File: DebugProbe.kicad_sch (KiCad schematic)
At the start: 36 parts, among them J5 DBG_PRGM, J6 UART_DBG, J7 DGB Exp. Header, U4 25Q32, U5 RP2040, Y1 12MHz

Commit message: Renamed files.
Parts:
- J5: symbol rp2040-launchpad-PCB:Jumper -> rp2350b-launchpad-PCB:Jumper
- U4: symbol rp2040-launchpad-PCB:25Q32 -> rp2350b-launchpad-PCB:25Q32
- U5: symbol rp2040-launchpad-PCB:RP2040 -> rp2350b-launchpad-PCB:RP2040
- USB1: symbol rp2040-launchpad-PCB:USB-C-Socket -> rp2350b-launchpad-PCB:USB-C-Socket
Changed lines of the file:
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@@
 	)
 	(symbol
-		(lib_id "rp2040-launchpad-PCB:25Q32")
+		(lib_id "rp2350b-launchpad-PCB:25Q32")
 		(at 93.98 135.89 0)
 		(mirror y)
@@
 	)
 	(symbol
-		(lib_id "rp2040-launchpad-PCB:RP2040")
+		(lib_id "rp2350b-launchpad-PCB:RP2040")
 		(at 139.7 105.41 0)
 		(unit 1)
@@
 	)
 	(symbol
-		(lib_id "rp2040-launchpad-PCB:Jumper")
+		(lib_id "rp2350b-launchpad-PCB:Jumper")
 		(at 102.87 151.13 0)
 		(unit 1)
@@
 	)
 	(symbol
-		(lib_id "rp2040-launchpad-PCB:+3V3_DBG")
+		(lib_id "rp2350b-launchpad-PCB:+3V3_DBG")
 		(at 196.85 52.07 0)
 		(unit 1)
@@
 	)
 	(symbol
-		(lib_id "rp2040-launchpad-PCB:GND_DBG")
+		(lib_id "rp2350b-launchpad-PCB:GND_DBG")
 		(at 223.52 85.09 0)
 		(unit 1)
@@
 	)
 	(symbol
-		(lib_id "rp2040-launchpad-PCB:+3V3_DBG")
+		(lib_id "rp2350b-launchpad-PCB:+3V3_DBG")
 		(at 80.01 128.27 0)
 		(unit 1)
@@
 	)
 	(symbol
-		(lib_id "rp2040-launchpad-PCB:GND_DBG")
+		(lib_id "rp2350b-launchpad-PCB:GND_DBG")
 		(at 88.9 59.69 0)
 		(unit 1)
@@
 	)
 	(symbol
-		(lib_id "rp2040-launchpad-PCB:GND_DBG")
+		(lib_id "rp2350b-launchpad-PCB:GND_DBG")
 		(at 80.01 152.4 0)
 		(unit 1)
@@
 	)
 	(symbol
-		(lib_id "rp2040-launchpad-PCB:GND_DBG")
+		(lib_id "rp2350b-launchpad-PCB:GND_DBG")
 		(at 134.62 152.4 0)
 		(unit 1)
@@
 	)
 	(symbol
-		(lib_id "rp2040-launchpad-PCB:GND_DBG")
+		(lib_id "rp2350b-launchpad-PCB:GND_DBG")
 		(at 120.65 59.69 0)
 		(unit 1)
@@
 	)
 	(symbol
-		(lib_id "rp2040-launchpad-PCB:GND_DBG")
+		(lib_id "rp2350b-launchpad-PCB:GND_DBG")
 		(at 80.01 110.49 0)
 		(unit 1)
@@
 	)
 	(symbol
-		(lib_id "rp2040-launchpad-PCB:+3V3_DBG")
+		(lib_id "rp2350b-launchpad-PCB:+3V3_DBG")
 		(at 143.51 151.13 270)
 		(unit 1)
@@
 	)
 	(symbol
-		(lib_id "rp2040-launchpad-PCB:GND_DBG")
+		(lib_id "rp2350b-launchpad-PCB:GND_DBG")
 		(at 99.06 104.14 90)
 		(unit 1)
@@
 	)
 	(symbol
-		(lib_id "rp2040-launchpad-PCB:GND_DBG")
+		(lib_id "rp2350b-launchpad-PCB:GND_DBG")
 		(at 212.09 123.19 180)
 		(unit 1)
@@
 	)
 	(symbol
-		(lib_id "rp2040-launchpad-PCB:+3V3_DBG")
+		(lib_id "rp2350b-launchpad-PCB:+3V3_DBG")
 		(at 196.85 123.19 0)
 		(unit 1)
@@
 	)
 	(symbol
-		(lib_id "rp2040-launchpad-PCB:+3V3_DBG")
+		(lib_id "rp2350b-launchpad-PCB:+3V3_DBG")
 		(at 113.03 121.92 90)
 		(unit 1)
@@
 	)
 	(symbol
-		(lib_id "rp2040-launchpad-PCB:+3V3_DBG")
+		(lib_id "rp2350b-launchpad-PCB:+3V3_DBG")
 		(at 119.38 151.13 270)
 		(unit 1)
@@
 	)
 	(symbol
-		(lib_id "rp2040-launchpad-PCB:GND_DBG")
+		(lib_id "rp2350b-launchpad-PCB:GND_DBG")
 		(at 196.85 59.69 0)
 		(unit 1)
@@
 		)
 		(instances
-			(project "rp2040-launchpad-PCB"
+			(project "rp2350b-launchpad-PCB"
 				(path "/60290668-847e-40fe-8544-1cbbc26023b6/00000000-0000-0000-0000-00006225139f"
 					(reference "R6")
@@
 	)
 	(symbol
-		(lib_id "rp2040-launchpad-PCB:GND_DBG")
+		(lib_id "rp2350b-launchpad-PCB:GND_DBG")
 		(at 59.69 109.22 0)
 		(unit 1)
@@
 		)
 		(instances
-			(project "rp2040-launchpad-PCB"
+			(project "rp2350b-launchpad-PCB"
 				(path "/60290668-847e-40fe-8544-1cbbc26023b6/00000000-0000-0000-0000-00006225139f"
 					(reference "#PWR010")
@@
 		)
 		(instances
-			(project "rp2040-launchpad-PCB"
+			(project "rp2350b-launchpad-PCB"
 				(path "/60290668-847e-40fe-8544-1cbbc26023b6/00000000-0000-0000-0000-00006225139f"
 					(reference "R7")
@@
 		)
 		(instances
-			(project "rp2040-launchpad-PCB"
+			(project "rp2350b-launchpad-PCB"
 				(path "/60290668-847e-40fe-8544-1cbbc26023b6/00000000-0000-0000-0000-00006225139f"
 					(reference "R8")
@@
 	)
 	(symbol
-		(lib_id "rp2040-launchpad-PCB:USB-C-Socket")
+		(lib_id "rp2350b-launchpad-PCB:USB-C-Socket")
 		(at 57.15 87.63 0)
 		(unit 1)

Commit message: More fixes...
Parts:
- U5: footprint rp2350-launchpad:QFN40P700X700X90-57N -> rp2350b-launchpad-PCB:QFN40P700X700X90-57N
- USB1: footprint rp2350-launchpad:USB-C-GCT-USB4105 -> rp2350b-launchpad-PCB:USB-C-GCT-USB4105
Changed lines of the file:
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@@
 			)
 		)
-		(property "Footprint" "rp2350-launchpad:QFN40P700X700X90-57N"
+		(property "Footprint" "rp2350b-launchpad-PCB:QFN40P700X700X90-57N"
 			(at 179.07 99.06 0)
 			(effects
@@
 			)
 		)
-		(property "Footprint" "rp2350-launchpad:USB-C-GCT-USB4105"
+		(property "Footprint" "rp2350b-launchpad-PCB:USB-C-GCT-USB4105"
 			(at 59.69 78.74 0)
 			(effects

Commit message: Footprint cleanup.
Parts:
- U5: footprint rp2350b-launchpad-PCB:QFN40P700X700X90-57N -> Package_DFN_QFN:QFN-56-1EP_7x7mm_P0.4mm_EP3.2x3.2mm_ThermalVias
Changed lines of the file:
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@@
 			)
 		)
-		(property "Footprint" "rp2350b-launchpad-PCB:QFN40P700X700X90-57N"
+		(property "Footprint" "Package_DFN_QFN:QFN-56-1EP_7x7mm_P0.4mm_EP3.2x3.2mm_ThermalVias"
 			(at 179.07 99.06 0)
 			(effects

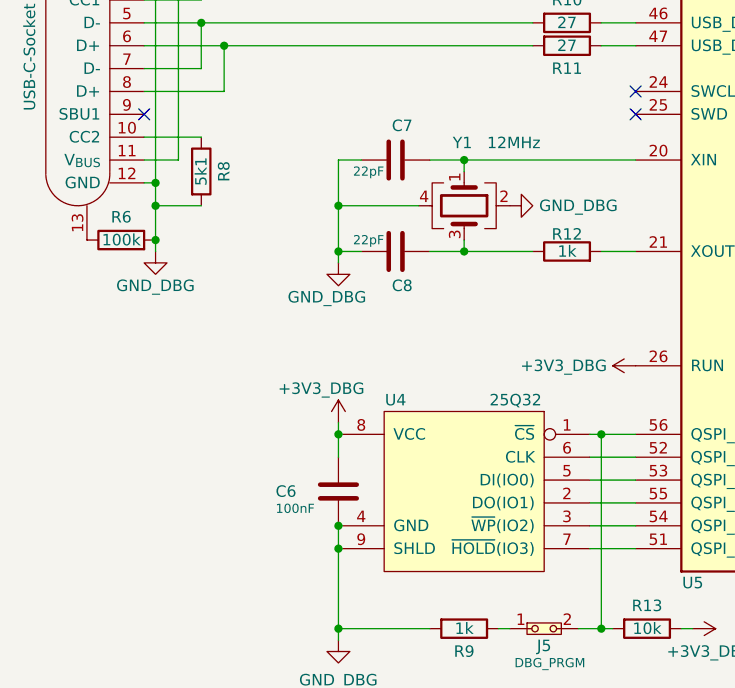
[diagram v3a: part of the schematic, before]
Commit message: Ready for Version v1.0. Changed PCB to comply with RPi design 'rules'. Without using special components and PCB designs, the PCB may not be produced :\
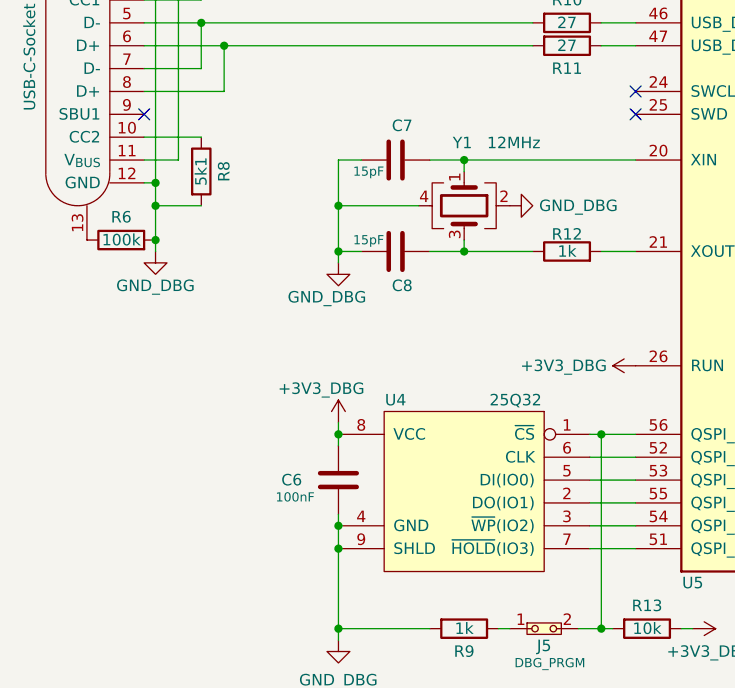
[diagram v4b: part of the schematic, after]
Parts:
- C7, C8: value 22pF -> 15pF
- U5: footprint Package_DFN_QFN:QFN-56-1EP_7x7mm_P0.4mm_EP3.2x3.2mm_ThermalVias -> Package_DFN_QFN:QFN-56-1EP_7x7mm_P0.4mm_EP3.2x3.2mm
- USB1: footprint rp2350b-launchpad-PCB:USB-C-GCT-USB4105 -> rp2350b-launchpad-PCB:GT-USB-7010B
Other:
- company: (none) -> ISS Intelligent Sensor Solutions
- title: (none) -> RP2350 Launchpad
- moved on the sheet: C6
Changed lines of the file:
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@@
 	(generator_version "8.0")
 	(paper "A4")
+	(title_block
+		(title "RP2350 Launchpad")
+		(date "2024-12-10")
+		(rev "v1.0")
+		(company "ISS Intelligent Sensor Solutions")
+		(comment 1 "(C) 2024 A. Terstegge")
+		(comment 2 "and integrated RP2040-based debugger")
+		(comment 3 "A TI-style Launchpad with RP2350 MCU")
+	)
 	(junction
 		(at 64.77 83.82)
@@
 	)
 	(junction
+		(at 80.01 129.54)
+		(diameter 0)
+		(color 0 0 0 0)
+	)
+	(junction
 		(at 137.16 52.07)
 		(diameter 0)
@@
 	)
 	(junction
-		(at 80.01 139.7)
-		(diameter 0)
-		(color 0 0 0 0)
-	)
-	(junction
 		(at 177.8 52.07)
 		(diameter 0)
@@
 	)
 	(junction
-		(at 165.1 59.69)
+		(at 80.01 139.7)
 		(diameter 0)
 		(color 0 0 0 0)
 	)
 	(junction
-		(at 190.5 52.07)
+		(at 165.1 59.69)
 		(diameter 0)
 		(color 0 0 0 0)
 	)
 	(junction
-		(at 109.22 151.13)
+		(at 190.5 52.07)
 		(diameter 0)
 		(color 0 0 0 0)
 	)
 	(junction
-		(at 95.25 59.69)
+		(at 109.22 151.13)
 		(diameter 0)
 		(color 0 0 0 0)
 	)
 	(junction
-		(at 80.01 129.54)
+		(at 95.25 59.69)
 		(diameter 0)
 		(color 0 0 0 0)
@@
 	(wire
 		(pts
+			(xy 80.01 129.54) (xy 80.01 130.81)
+		)
+		(stroke
+			(width 0)
+			(type default)
+		)
+	)
+	(wire
+		(pts
 			(xy 59.69 104.14) (xy 64.77 104.14)
 		)
@@
 	(wire
 		(pts
-			(xy 80.01 132.08) (xy 80.01 129.54)
-		)
-		(stroke
-			(width 0)
-			(type default)
-		)
-	)
-	(wire
-		(pts
 			(xy 210.82 139.7) (xy 222.25 139.7)
 		)
@@
 	(wire
 		(pts
+			(xy 80.01 138.43) (xy 80.01 139.7)
+		)
+		(stroke
+			(width 0)
+			(type default)
+		)
+	)
+	(wire
+		(pts
 			(xy 107.95 139.7) (xy 113.03 139.7)
 		)
@@
 	(symbol
 		(lib_id "Device:C")
-		(at 80.01 135.89 0)
+		(at 80.01 134.62 0)
 		(unit 1)
 		(exclude_from_sim no)
@@
 		(dnp no)
 		(property "Reference" "C6"
-			(at 73.025 135.89 0)
+			(at 73.66 134.62 0)
 			(effects
 				(font
@@
 		)
 		(property "Value" "100nF"
-			(at 73.025 137.795 0)
+			(at 73.025 136.525 0)
 			(effects
 				(font
@@
 		)
 		(property "Footprint" "Capacitor_SMD:C_0603_1608Metric"
-			(at 80.01 135.89 0)
+			(at 80.01 134.62 0)
 			(effects
 				(font
@@
 		)
 		(property "Datasheet" "https://www.digikey.de/de/products/detail/kemet/C0603C104J4RAC7013/8572406"
-			(at 80.01 135.89 0)
+			(at 80.01 134.62 0)
 			(effects
 				(font
@@
 		)
 		(property "Description" ""
-			(at 80.01 135.89 0)
+			(at 80.01 134.62 0)
 			(effects
 				(font
@@
 		)
 		(property "MANUFACTURER" "z.B. Kemet"
-			(at 80.01 135.89 0)
+			(at 80.01 134.62 0)
 			(effects
 				(font
@@
 		)
 		(property "STANDARD" "unkritisch"
-			(at 80.01 135.89 0)
+			(at 80.01 134.62 0)
 			(effects
 				(font
@@
 			)
 		)
-		(property "Footprint" "Package_DFN_QFN:QFN-56-1EP_7x7mm_P0.4mm_EP3.2x3.2mm_ThermalVias"
+		(property "Footprint" "Package_DFN_QFN:QFN-56-1EP_7x7mm_P0.4mm_EP3.2x3.2mm"
 			(at 179.07 99.06 0)
 			(effects
@@
 			)
 		)
-		(property "Value" "22pF"
+		(property "Value" "15pF"
 			(at 85.09 107.95 90)
 			(effects
@@
 			)
 		)
-		(property "Value" "22pF"
+		(property "Value" "15pF"
 			(at 85.09 100.33 90)
 			(effects
@@
 			)
 		)
-		(property "Footprint" "rp2350b-launchpad-PCB:USB-C-GCT-USB4105"
+		(property "Footprint" "rp2350b-launchpad-PCB:GT-USB-7010B"
 			(at 59.69 78.74 0)
 			(effects

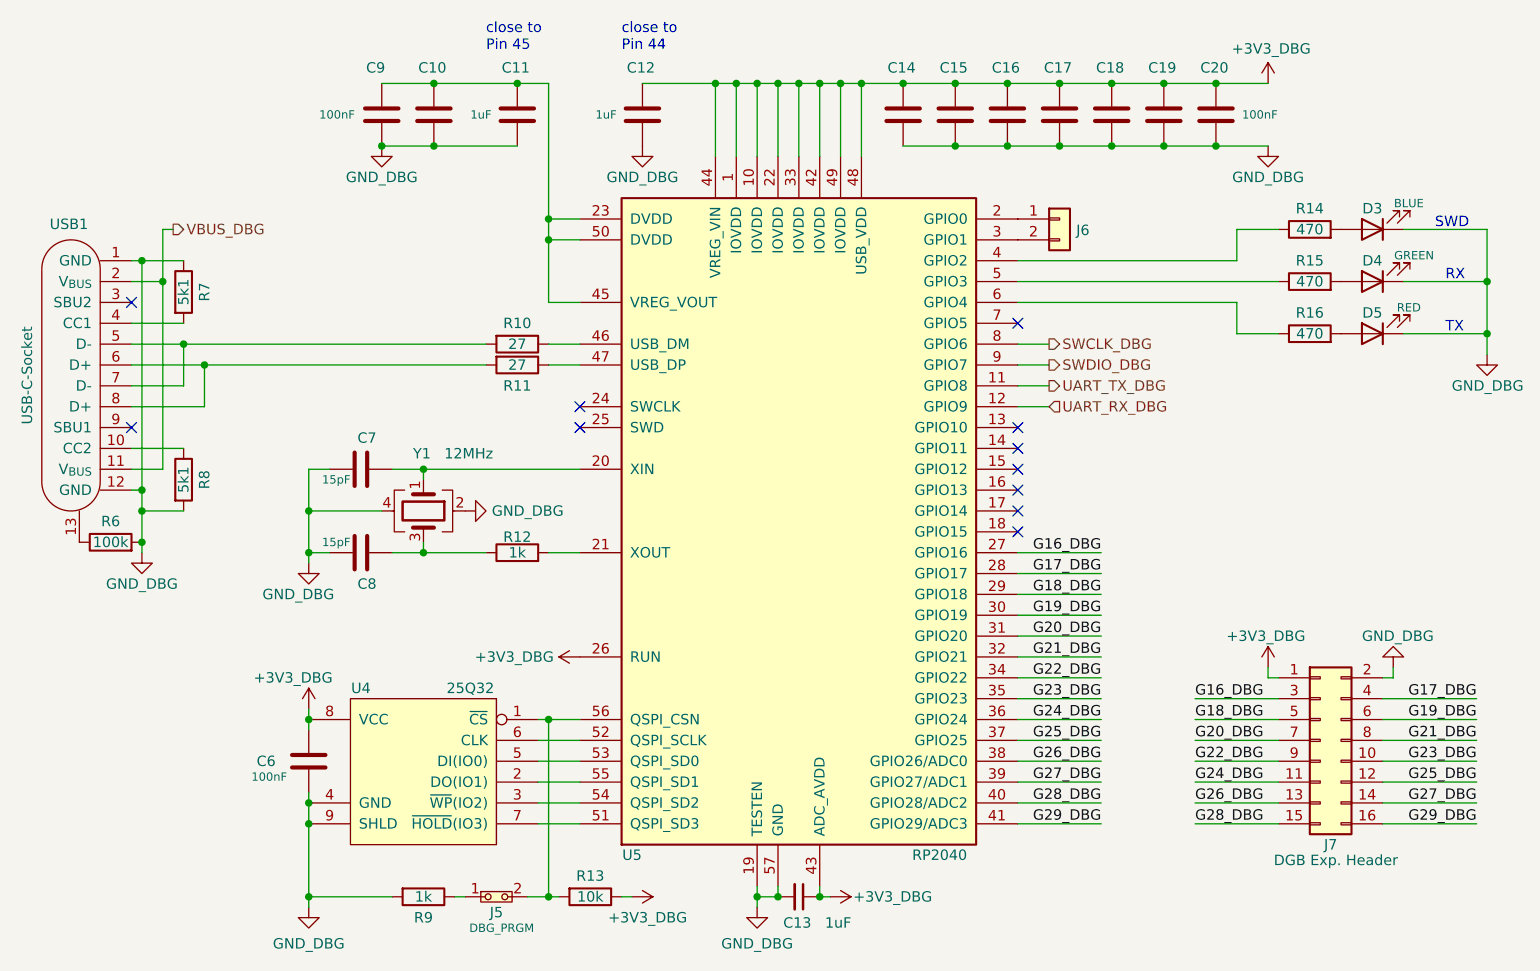
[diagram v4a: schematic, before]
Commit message: Updates for better JLCPCB processing. Version is now 1.1
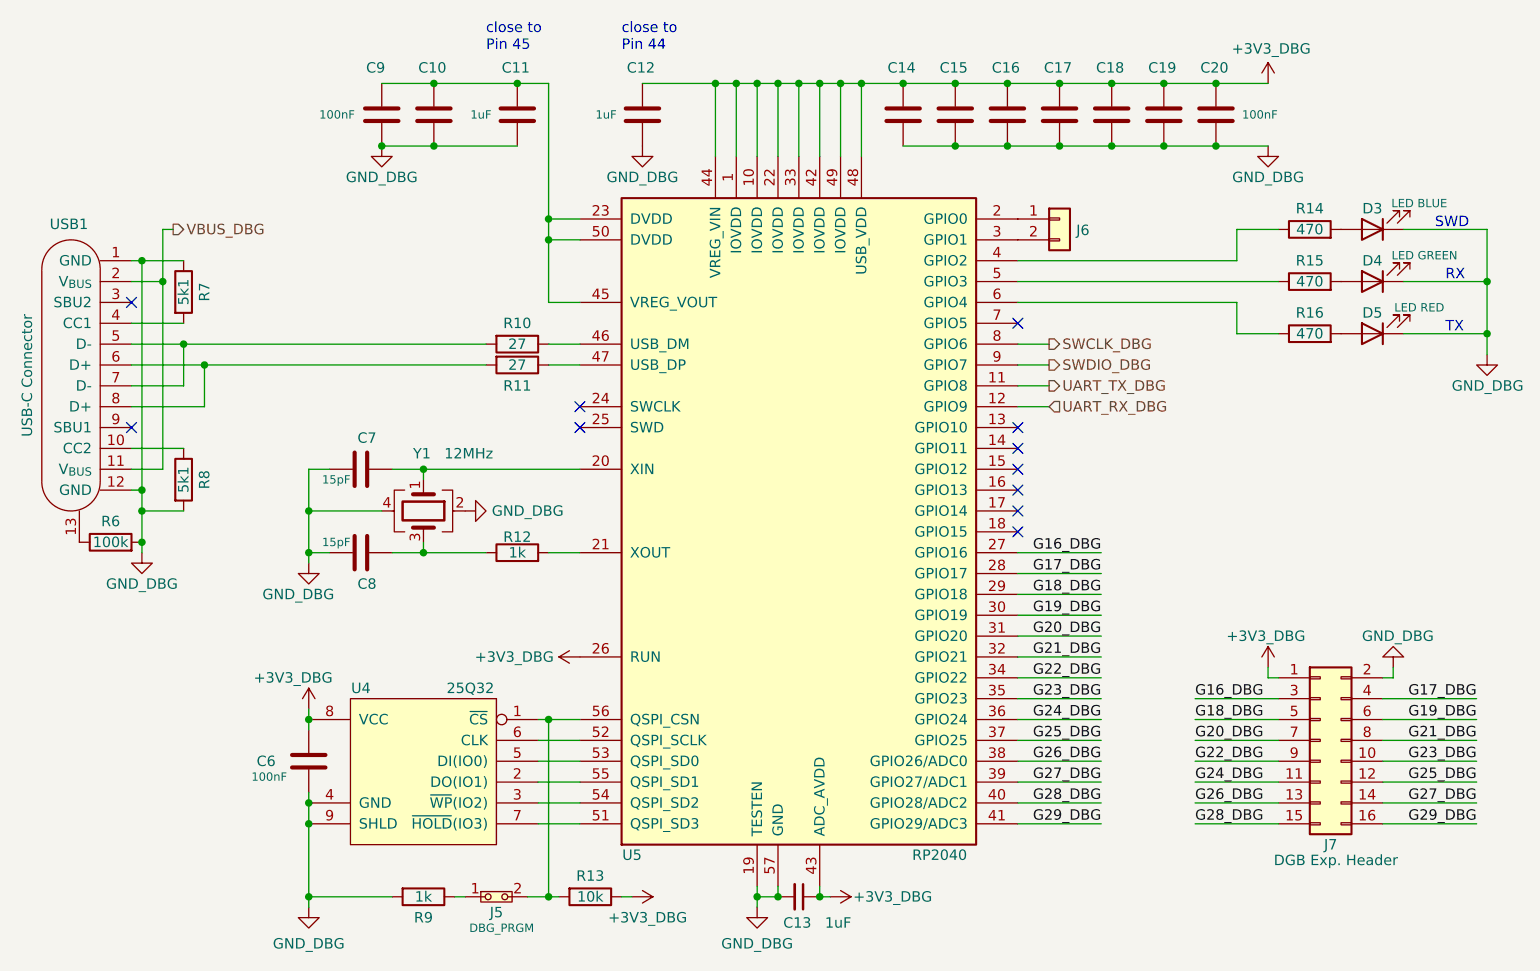
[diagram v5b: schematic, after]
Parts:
- C10, C14, C15, C16, C17, C18, C19, C20, C6, C9: Hersteller (none) -> YAGEO; JLCPCB Part # (none) -> C14663
- C11, C12, C13: Hersteller (none) -> Samsung Electro-Mechanics; JLCPCB Part # (none) -> C15849
- C7, C8: Hersteller (none) -> Samsung Electro-Mechanics; JLCPCB Part # (none) -> C1644; MANUFACTURER z.B. Kemet -> (none); STANDARD unkritisch -> (none)
- D3: value BLUE -> LED BLUE; Hersteller (none) -> Hubei KENTO Elec; JLCPCB Part # (none) -> C2288; STANDARD unkritisch -> Hubei KENTO Elec
- D4: value GREEN -> LED GREEN; Hersteller (none) -> Hubei KENTO Elec; JLCPCB Part # (none) -> C12624; STANDARD unkritisch -> (none)
- D5: value RED -> LED RED; Hersteller (none) -> Hubei KENTO Elec; JLCPCB Part # (none) -> C2286; STANDARD unkritisch -> (none)
- R10, R11: Hersteller (none) -> UNI-ROYAL(Uniroyal Elec); JLCPCB Part # (none) -> C25190
- R12: Hersteller (none) -> UNI-ROYAL(Uniroyal Elec); JLCPCB Part # (none) -> C21190
- R13: Hersteller (none) -> UNI-ROYAL(Uniroyal Elec); JLCPCB Part # (none) -> C25804; STANDARD unkritisch -> (none)
- R14, R15, R16: Hersteller (none) -> UNI-ROYAL(Uniroyal Elec); JLCPCB Part # (none) -> C23179; STANDARD unkritisch -> (none)
- R6: Hersteller (none) -> UNI-ROYAL(Uniroyal Elec); JLCPCB Part # (none) -> C25803; STANDARD unkritisch -> (none)
- R7, R8: Hersteller (none) -> UNI-ROYAL(Uniroyal Elec); JLCPCB Part # (none) -> C23186
- R9: Hersteller (none) -> UNI-ROYAL(Uniroyal Elec); JLCPCB Part # (none) -> C21190; STANDARD unkritisch -> (none)
- U4: Hersteller (none) -> Winbond Elec; JLCPCB Part # (none) -> C571260
- U5: Hersteller (none) -> Raspberry Pi; JLCPCB Part # (none) -> C2040
- USB1: value USB-C-Socket -> USB-C Connector; Hersteller (none) -> G-Switch; JLCPCB Part # (none) -> C2837092
- Y1: footprint Crystal:Crystal_SMD_TXC_7M-4Pin_3.2x2.5mm -> Crystal:Crystal_SMD_Abracon_ABM8AIG-4Pin_3.2x2.5mm; Hersteller (none) -> Abracon LLC; JLCPCB Part # (none) -> C20625731
